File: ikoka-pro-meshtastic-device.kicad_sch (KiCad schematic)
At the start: 32 parts, among them J10 BWSMA-KWE-Z001, J2 Conn_ARM_JTAG_SWD_10, J3 BWSMA-KWE-Z001, J8 USB_C_Receptacle_USB2.0_16P, SW2 TS36CA-0.6, U3 L76K, U4 E22-900M30S, U5 nRF52840_E73-2G4M08S1C, U6 XC6206P332MR

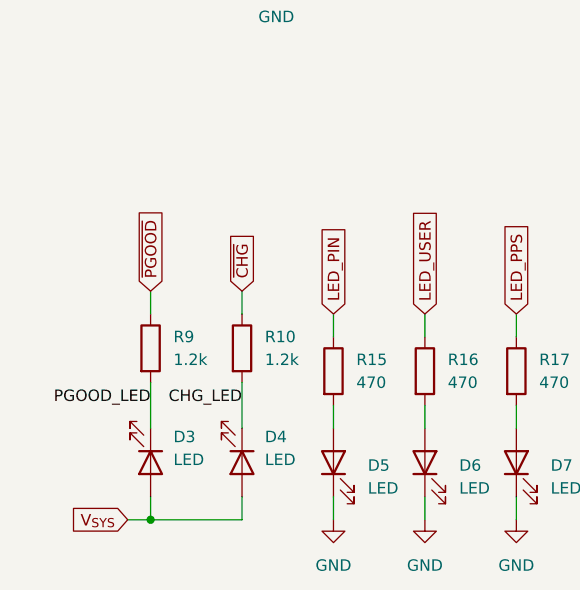
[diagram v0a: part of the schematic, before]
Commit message: feat: Move SWD pads further away from USB-C and battery
Signed-off-by: Andrew Yong <me@ndoo.sg>
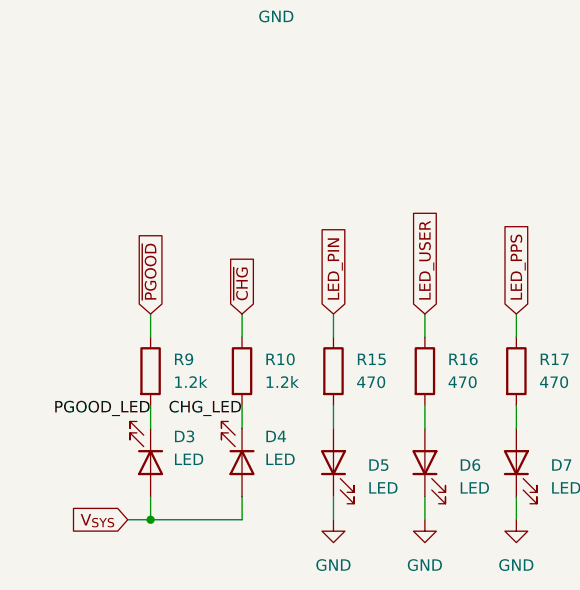
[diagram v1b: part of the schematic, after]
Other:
- moved on the sheet: R10, R9
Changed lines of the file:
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@@
 	(wire
 		(pts
-			(xy 27.94 166.37) (xy 27.94 171.45)
+			(xy 27.94 168.91) (xy 27.94 171.45)
 		)
 		(stroke
@@
 	(wire
 		(pts
-			(xy 38.1 156.21) (xy 38.1 158.75)
+			(xy 38.1 158.75) (xy 38.1 161.29)
 		)
 		(stroke
@@
 	(wire
 		(pts
-			(xy 38.1 166.37) (xy 38.1 171.45)
+			(xy 38.1 168.91) (xy 38.1 171.45)
 		)
 		(stroke
@@
 	(wire
 		(pts
-			(xy 27.94 156.21) (xy 27.94 158.75)
+			(xy 27.94 158.75) (xy 27.94 161.29)
 		)
 		(stroke
@@
 	)
 	(label "CHG_LED"
-		(at 38.1 168.91 180)
+		(at 38.1 170.18 180)
 		(effects
 			(font
@@
 	)
 	(label "PGOOD_LED"
-		(at 27.94 168.91 180)
+		(at 27.94 170.18 180)
 		(effects
 			(font
@@
 	(global_label "~{PGOOD}"
 		(shape input)
-		(at 27.94 156.21 90)
+		(at 27.94 158.75 90)
 		(fields_autoplaced yes)
 		(effects
@@
 		)
 		(property "Intersheetrefs" "${INTERSHEET_REFS}"
-			(at 27.94 146.7538 90)
+			(at 27.94 149.2938 90)
 			(effects
 				(font
@@
 	(global_label "~{CHG}"
 		(shape input)
-		(at 38.1 156.21 90)
+		(at 38.1 158.75 90)
 		(fields_autoplaced yes)
 		(effects
@@
 		)
 		(property "Intersheetrefs" "${INTERSHEET_REFS}"
-			(at 38.1 149.3543 90)
+			(at 38.1 151.8943 90)
 			(effects
 				(font
@@
 	(symbol
 		(lib_id "Device:R")
-		(at 38.1 162.56 0)
+		(at 38.1 165.1 0)
 		(unit 1)
 		(exclude_from_sim no)
@@
 		(dnp no)
 		(property "Reference" "R10"
-			(at 40.64 161.2899 0)
+			(at 40.64 163.8299 0)
 			(effects
 				(font
@@
 		)
 		(property "Value" "1.2k"
-			(at 40.64 163.8299 0)
+			(at 40.64 166.3699 0)
 			(effects
 				(font
@@
 		)
 		(property "Footprint" "Resistor_SMD:R_0402_1005Metric"
-			(at 36.322 162.56 90)
+			(at 36.322 165.1 90)
 			(effects
 				(font
@@
 		)
 		(property "Datasheet" "~"
-			(at 38.1 162.56 0)
+			(at 38.1 165.1 0)
 			(effects
 				(font
@@
 		)
 		(property "Description" "Resistor"
-			(at 38.1 162.56 0)
+			(at 38.1 165.1 0)
 			(effects
 				(font
@@
 	(symbol
 		(lib_id "Device:R")
-		(at 27.94 162.56 0)
+		(at 27.94 165.1 0)
 		(unit 1)
 		(exclude_from_sim no)
@@
 		(dnp no)
 		(property "Reference" "R9"
-			(at 30.48 161.2899 0)
+			(at 30.48 163.8299 0)
 			(effects
 				(font
@@
 		)
 		(property "Value" "1.2k"
-			(at 30.48 163.8299 0)
+			(at 30.48 166.3699 0)
 			(effects
 				(font
@@
 		)
 		(property "Footprint" "Resistor_SMD:R_0402_1005Metric"
-			(at 26.162 162.56 90)
+			(at 26.162 165.1 90)
 			(effects
 				(font
@@
 		)
 		(property "Datasheet" "~"
-			(at 27.94 162.56 0)
+			(at 27.94 165.1 0)
 			(effects
 				(font
@@
 		)
 		(property "Description" "Resistor"
-			(at 27.94 162.56 0)
+			(at 27.94 165.1 0)
 			(effects
 				(font

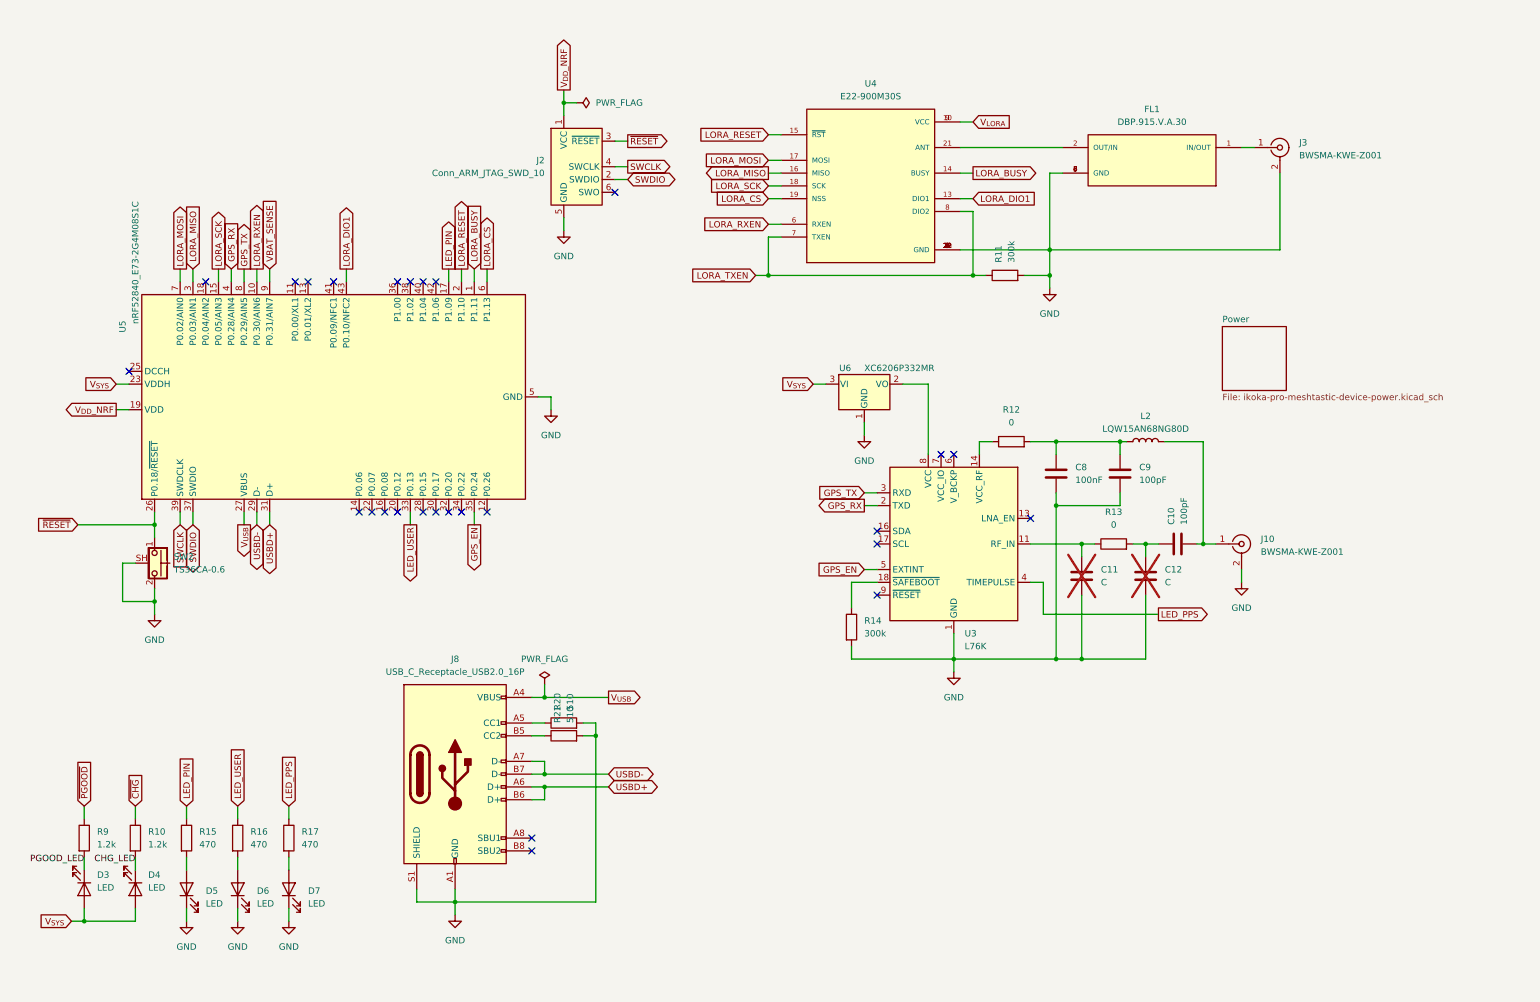
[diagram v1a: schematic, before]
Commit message: feat: I2C and 100k+300k VBAT divider
Fixes #1

Signed-off-by: Andrew Yong <me@ndoo.sg>
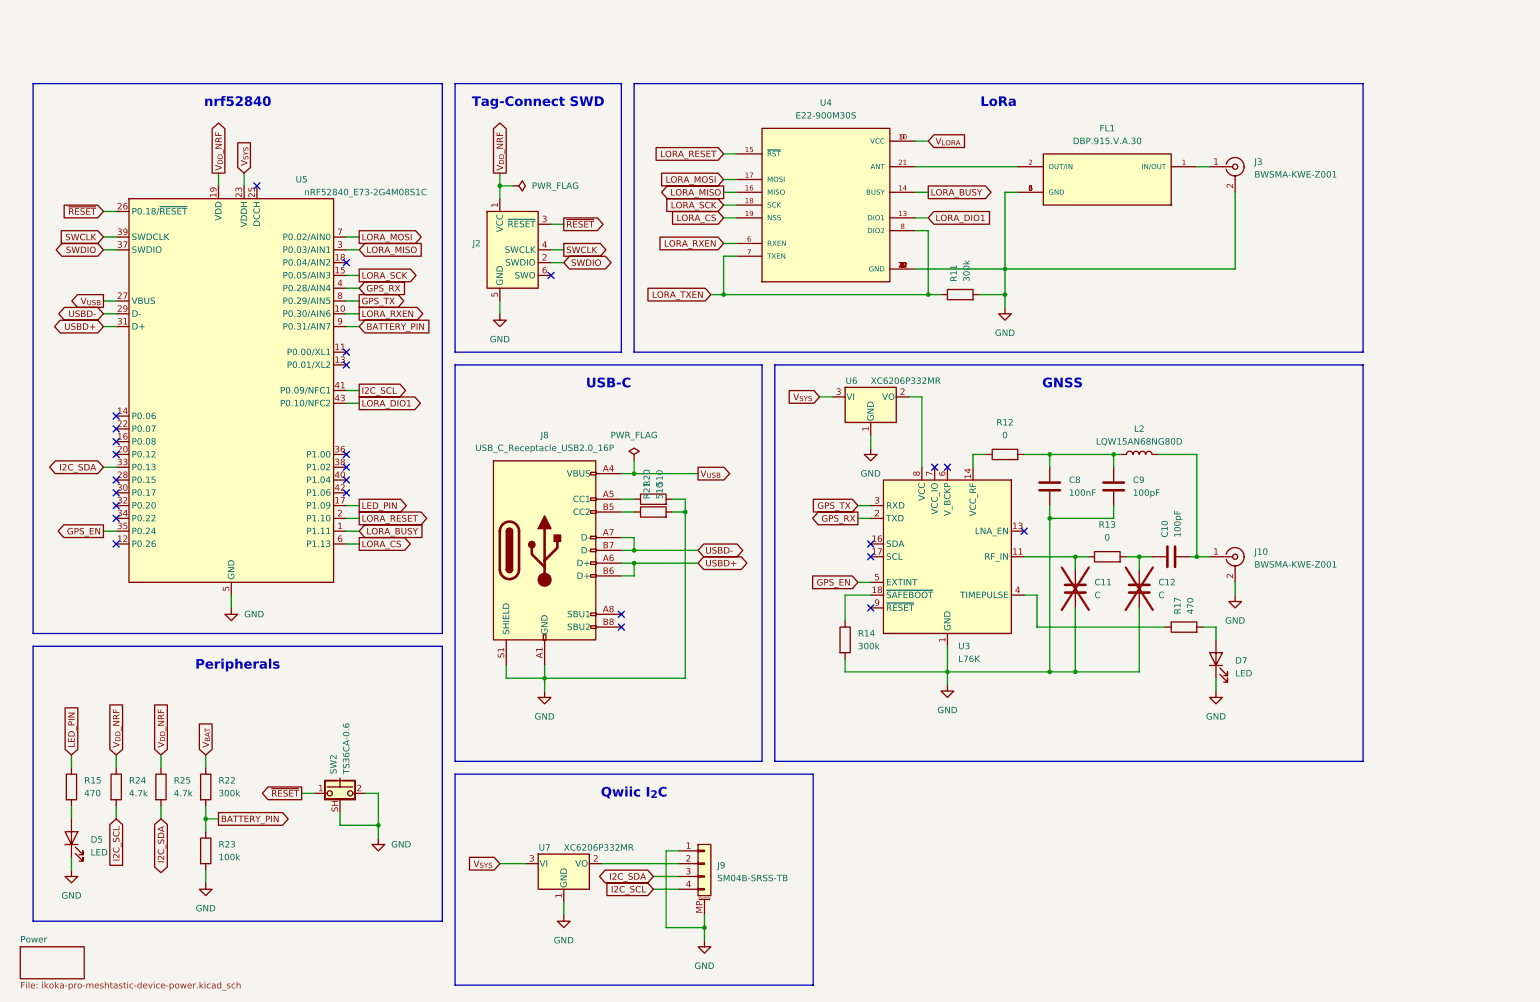
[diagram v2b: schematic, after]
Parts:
- removed D3, D4, D6: LED, LED_SMD:LED_0603_1608Metric, symbol Device:LED
- removed R10, R9: 1.2k, Resistor_SMD:R_0402_1005Metric, symbol Device:R
- removed R16: 470, Resistor_SMD:R_0402_1005Metric, symbol Device:R
- added J9: SM04B-SRSS-TB, Connector_JST:JST_SH_SM04B-SRSS-TB_1x04-1MP_P1.00mm_Horizontal, symbol Connector_Generic_MountingPin:Conn_01x04_MountingPin
- added R22: 300k, Resistor_SMD:R_0402_1005Metric, symbol Device:R
- added R23: 100k, Resistor_SMD:R_0402_1005Metric, symbol Device:R
- added R24, R25: 4.7k, Resistor_SMD:R_0402_1005Metric, symbol Device:R
- added U7: XC6206P332MR, Package_TO_SOT_SMD:SOT-23-3, symbol Regulator_Linear:XC6206PxxxMR
- C10, C9: LCSC C59461 -> C1546
- C8: LCSC C59461 -> C307331
- J10: LCSC (none) -> C496551
- J8: LCSC (none) -> C2843970
- L2: LCSC (none) -> C3221844
- R11, R14: LCSC (none) -> C25774
- R12, R13: LCSC (none) -> C17168
- R15, R17: LCSC (none) -> C25117
- R20, R21: LCSC (none) -> C25123
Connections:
- net GND: now also J9.1 (Pin_1), J9.MP (MountPin), R23.2, U7.1 (GND)
- net V_{DD}_NRF: now also R24.1, R25.1
- net V_{SYS}: now also U7.3 (VI)
- net I2C_SCL: now reaches U5.41 (P0.09/NFC1)
- net I2C_SCL: now also J9.4 (Pin_4), R24.2
- net LED_PPS: no longer names the net of R17.1, U3.4 (TIMEPULSE)
- net LED_USER renamed I2C_SDA
- net I2C_SDA: now also J9.3 (Pin_3), R25.2
- net VBAT_SENSE renamed BATTERY_PIN
- net BATTERY_PIN: now also R22.2, R23.1
- new net: J9.2 (Pin_2), U7.2 (VO)
- new net V_{BAT}: R22.1
- no-connect marks 27 -> 26
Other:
- note added: "GNSS"
- note added: "LoRa"
- note added: "Peripherals"
- note added: "Qwiic I_{2}C"
- note added: "Tag-Connect SWD"
- note added: "USB-C"
- note added: "nrf52840"
- moved on the sheet: C10, C11, C12, C8, C9, D5, D7, FL1, J10, J2, J3, J8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

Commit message: fix: 4.7kΩ I2C pull-up JLCPCB part selection
Signed-off-by: Andrew Yong <me@ndoo.sg>
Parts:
- R24, R25: LCSC C17168 -> C25900
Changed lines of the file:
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@@
 			)
 		)
-		(property "LCSC" "C17168"
+		(property "LCSC" "C25900"
 			(at 49.53 154.94 0)
 			(effects
@@
 			)
 		)
-		(property "LCSC" "C17168"
+		(property "LCSC" "C25900"
 			(at 40.64 154.94 0)
 			(effects

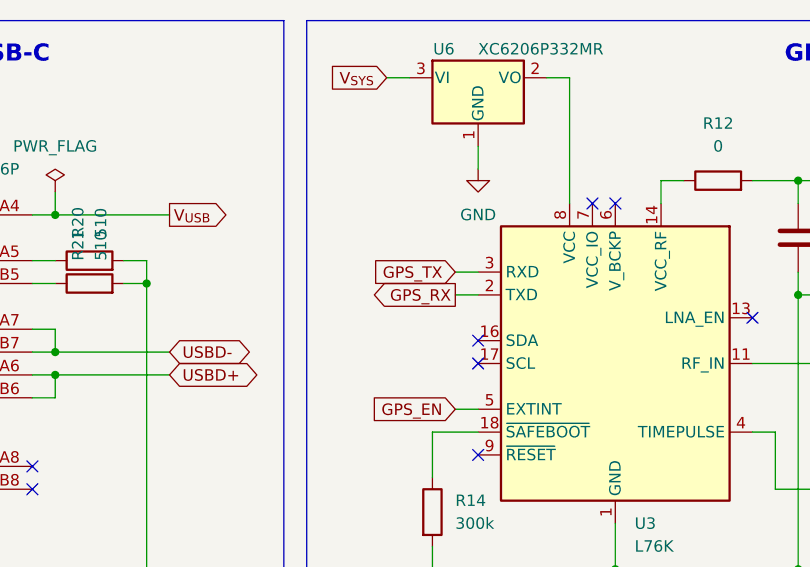
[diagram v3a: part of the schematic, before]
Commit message: fix: Swap GPS Tx and Rx (fixes #5)
Signed-off-by: Andrew Yong <me@ndoo.sg>
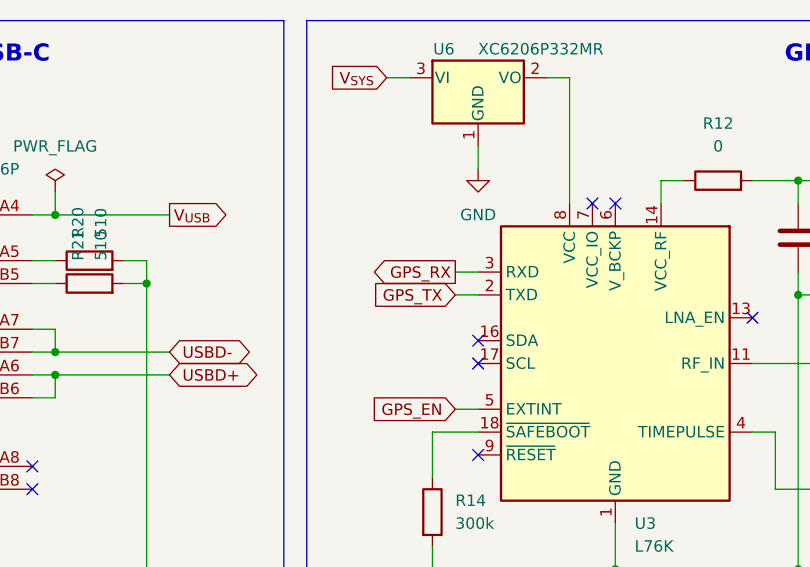
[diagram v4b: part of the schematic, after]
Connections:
- net GPS_RX: now also U3.3 (RXD); no longer U3.2 (TXD)
- net GPS_TX: now also U3.2 (TXD); no longer U3.3 (RXD)
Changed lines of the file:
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@@
-		)
-	)
-	(global_label "GPS_TX"
-		(shape input)
-		(at 181.61 99.06 180)
-		(fields_autoplaced yes)
-		(effects
-			(font
-				(size 1.27 1.27)
-			)
-			(justify right)
-		)
-		(property "Intersheetrefs" "${INTERSHEET_REFS}"
-			(at 171.7306 99.06 0)
-			(effects
-				(font
-					(size 1.27 1.27)
-				)
-				(justify right)
-				(hide yes)
-			)
 		)
 	)
@@
 		)
 	)
-	(global_label "GPS_RX"
-		(shape output)
-		(at 181.61 101.6 180)
-		(fields_autoplaced yes)
-		(effects
-			(font
-				(size 1.27 1.27)
-			)
-			(justify right)
-		)
-		(property "Intersheetrefs" "${INTERSHEET_REFS}"
-			(at 171.4282 101.6 0)
-			(effects
-				(font
-					(size 1.27 1.27)
-				)
-				(justify right)
-				(hide yes)
-			)
-		)
-	)
 	(global_label "LORA_RXEN"
 		(shape input)
@@
 		)
 	)
+	(global_label "GPS_RX"
+		(shape output)
+		(at 181.61 99.06 180)
+		(fields_autoplaced yes)
+		(effects
+			(font
+				(size 1.27 1.27)
+			)
+			(justify right)
+		)
+		(property "Intersheetrefs" "${INTERSHEET_REFS}"
+			(at 171.4282 99.06 0)
+			(effects
+				(font
+					(size 1.27 1.27)
+				)
+				(justify right)
+				(hide yes)
+			)
+		)
+	)
 	(global_label "V_{DD}_NRF"
 		(shape input)
@@
 				(hide yes)
 			)
+		)
+	)
+	(global_label "GPS_TX"
+		(shape input)
+		(at 181.61 101.6 180)
+		(fields_autoplaced yes)
+		(effects
+			(font
+				(size 1.27 1.27)
+			)
+			(justify right)
+		)
+		(property "Intersheetrefs" "${INTERSHEET_REFS}"
+			(at 171.7306 101.6 0)
+			(effects
+				(font
+					(size 1.27 1.27)
+				)
+				(justify right)
+				(hide yes)
+			)

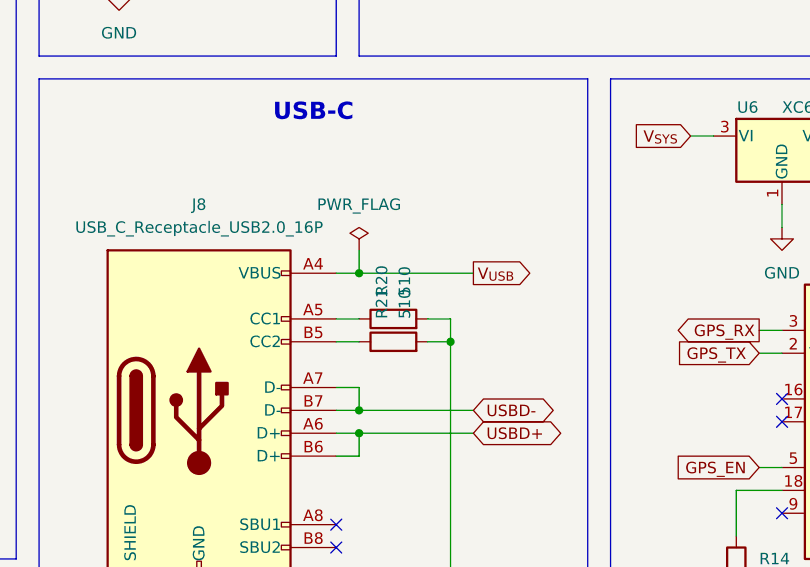
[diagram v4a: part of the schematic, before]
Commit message: fix: Change USB-C CC resistors from 510Ω to 5.1kΩ (fixes #8)
Signed-off-by: Andrew Yong <me@ndoo.sg>
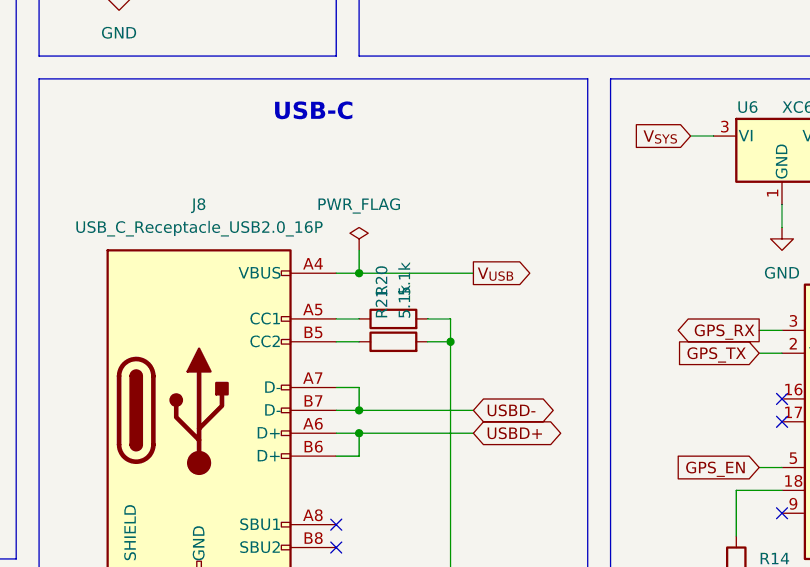
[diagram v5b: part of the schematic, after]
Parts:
- R20, R21: value 510 -> 5.1k; LCSC C25123 -> C25905
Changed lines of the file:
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@@
 			)
 		)
-		(property "Value" "510"
+		(property "Value" "5.1k"
 			(at 142.2399 97.79 0)
 			(effects
@@
 			)
 		)
-		(property "LCSC" "C25123"
+		(property "LCSC" "C25905"
 			(at 139.6999 97.79 0)
 			(effects
@@
 			)
 		)
-		(property "Value" "510"
+		(property "Value" "5.1k"
 			(at 142.2399 95.25 0)
 			(effects
@@
 			)
 		)
-		(property "LCSC" "C25123"
+		(property "LCSC" "C25905"
 			(at 139.6999 95.25 0)
 			(effects
